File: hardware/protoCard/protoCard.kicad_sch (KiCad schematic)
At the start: 2 parts, among them J1 6502 Edge, J2 6502 Pinheader

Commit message: Protoboard v1.0
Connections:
- net NC36 is gone; now on net ~{RAM_CS}: J1.36 (Pin_36), J2.36 (Pin_36)
- net NC38 is gone; now on net A8: J1.38 (Pin_38), J2.38 (Pin_38)
- net NC40 is gone; now on net A10: J1.40 (Pin_40), J2.40 (Pin_40)
- net NC41 is gone; now on net A11: J1.41 (Pin_41), J2.41 (Pin_41)
- net ~{R0M_CS} is gone; now on net ~{NMI}: J1.19 (Pin_19), J2.19 (Pin_19)
- net A0: now also J1.6 (Pin_6), J2.6 (Pin_6); no longer J1.2 (Pin_2), J2.2 (Pin_2)
- net A1: now also J1.7 (Pin_7), J2.7 (Pin_7); no longer J1.3 (Pin_3), J2.3 (Pin_3)
- net A10: no longer J1.44 (Pin_44), J2.44 (Pin_44)
- net A11: no longer J1.45 (Pin_45), J2.45 (Pin_45)
- net A12: now also J1.42 (Pin_42), J2.42 (Pin_42); no longer J1.46 (Pin_46), J2.46 (Pin_46)
- net A13: now also J1.43 (Pin_43), J2.43 (Pin_43); no longer J1.47 (Pin_47), J2.47 (Pin_47)
- net A14: now also J1.44 (Pin_44), J2.44 (Pin_44); no longer J1.48 (Pin_48), J2.48 (Pin_48)
- net A15: now also J1.45 (Pin_45), J2.45 (Pin_45); no longer J1.49 (Pin_49), J2.49 (Pin_49)
- net A2: now also J1.8 (Pin_8), J2.8 (Pin_8); no longer J1.4 (Pin_4), J2.4 (Pin_4)
- net A3: now also J1.9 (Pin_9), J2.9 (Pin_9); no longer J1.5 (Pin_5), J2.5 (Pin_5)
- net A4: now also J1.10 (Pin_10), J2.10 (Pin_10); no longer J1.6 (Pin_6), J2.6 (Pin_6)
- net A5: now also J1.11 (Pin_11), J2.11 (Pin_11); no longer J1.7 (Pin_7), J2.7 (Pin_7)
- net A6: now also J1.12 (Pin_12), J2.12 (Pin_12); no longer J1.8 (Pin_8), J2.8 (Pin_8)
- net A7: now also J1.13 (Pin_13), J2.13 (Pin_13); no longer J1.9 (Pin_9), J2.9 (Pin_9)
- net A8: no longer J1.42 (Pin_42), J2.42 (Pin_42)
- net A9: now also J1.39 (Pin_39), J2.39 (Pin_39); no longer J1.43 (Pin_43), J2.43 (Pin_43)
- net D0: now also J1.5 (Pin_5), J2.5 (Pin_5); no longer J1.10 (Pin_10), J2.10 (Pin_10)
- net D1: now also J1.4 (Pin_4), J2.4 (Pin_4); no longer J1.11 (Pin_11), J2.11 (Pin_11)
- net D2: now also J1.3 (Pin_3), J2.3 (Pin_3); no longer J1.12 (Pin_12), J2.12 (Pin_12)
- net D3: now also J1.2 (Pin_2), J2.2 (Pin_2); no longer J1.13 (Pin_13), J2.13 (Pin_13)
- net D4: now also J1.49 (Pin_49), J2.49 (Pin_49); no longer J1.14 (Pin_14), J2.14 (Pin_14)
- net D5: now also J1.48 (Pin_48), J2.48 (Pin_48); no longer J1.15 (Pin_15), J2.15 (Pin_15)
- net D6: now also J1.47 (Pin_47), J2.47 (Pin_47); no longer J1.16 (Pin_16), J2.16 (Pin_16)
- net D7: now also J1.46 (Pin_46), J2.46 (Pin_46); no longer J1.17 (Pin_17), J2.17 (Pin_17)
- net GND: no longer J1.39 (Pin_39), J2.39 (Pin_39)
- net ~{IO_CS}: now also J1.20 (Pin_20), J2.20 (Pin_20); no longer J1.21 (Pin_21), J2.21 (Pin_21)
- net ~{NMI}: no longer J1.20 (Pin_20), J2.20 (Pin_20)
- net ~{RAM_CS}: no longer J1.33 (Pin_33), J2.33 (Pin_33)
- net ~{RD}: now also J1.16 (Pin_16), J2.16 (Pin_16); no longer J1.34 (Pin_34), J2.34 (Pin_34)
- new net NC14: J1.14 (Pin_14), J2.14 (Pin_14)
- new net NC15: J1.15 (Pin_15), J2.15 (Pin_15)
- new net NC33: J1.33 (Pin_33), J2.33 (Pin_33)
- new net NC34: J1.34 (Pin_34), J2.34 (Pin_34)
- new net ~{IO_08}: J1.21 (Pin_21), J2.21 (Pin_21)
- new net ~{ROM_CS}: J1.17 (Pin_17), J2.17 (Pin_17)
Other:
- company: (none) -> MDS
- title: (none) -> Protoboard Card

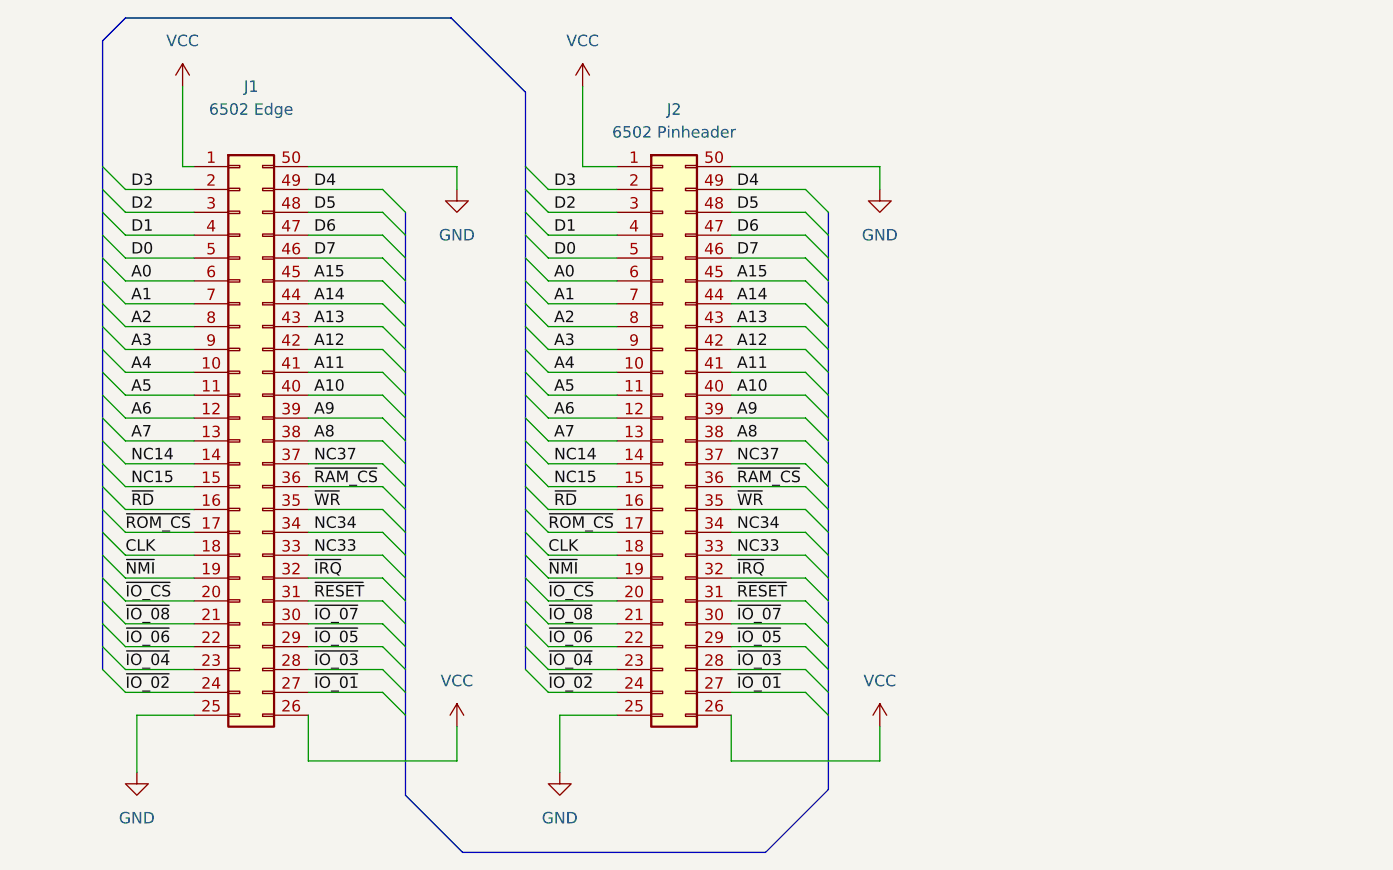
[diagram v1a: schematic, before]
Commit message: fixed pinout + power led
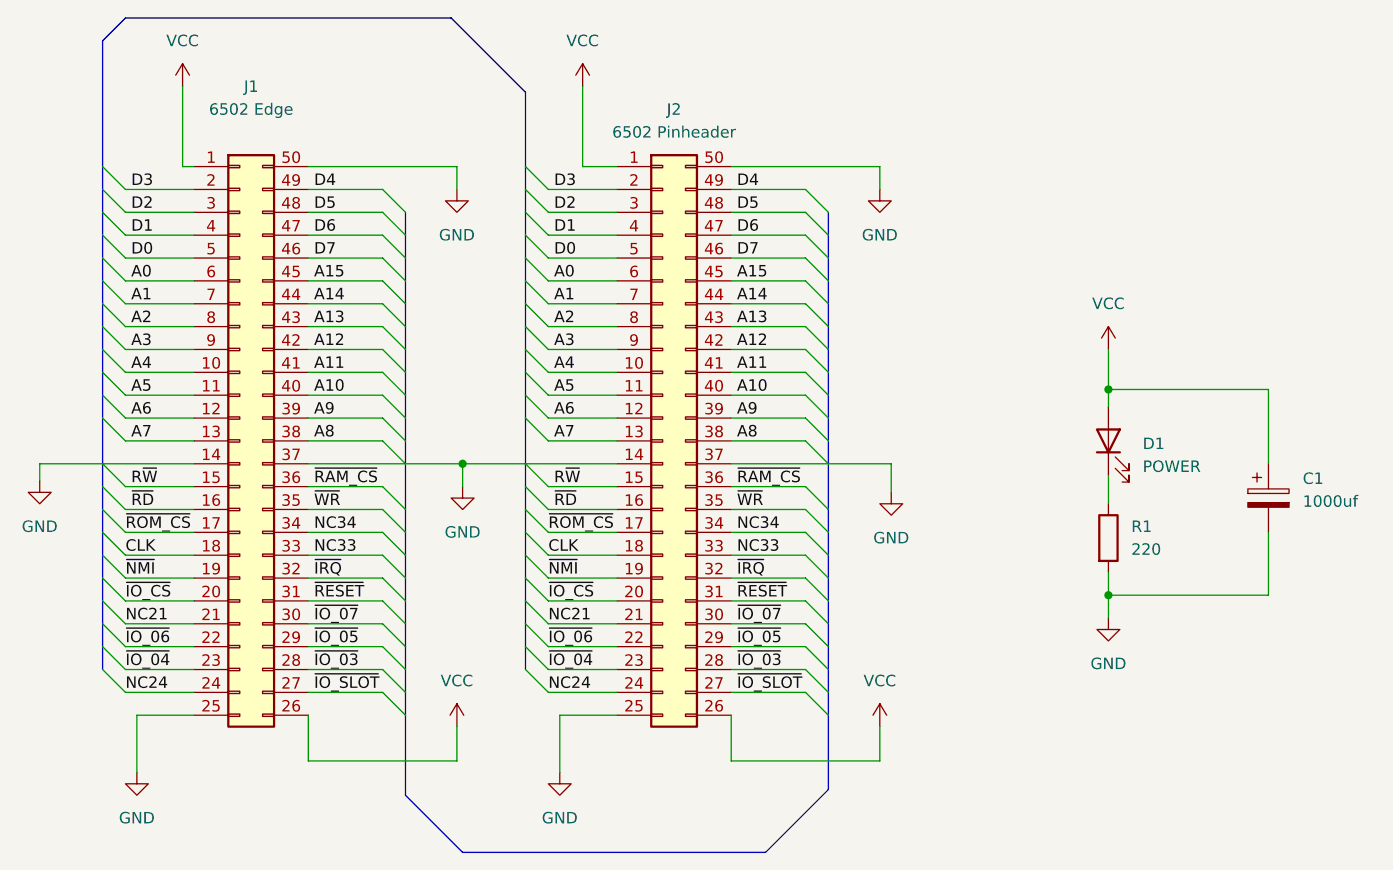
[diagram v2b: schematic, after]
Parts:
- added C1: 1000uf, Capacitor_THT:CP_Radial_D5.0mm_P2.50mm, symbol Device:C_Polarized
- added D1: POWER, LED_THT:LED_D3.0mm, symbol Device:LED
- added R1: 220, Resistor_THT:R_Axial_DIN0207_L6.3mm_D2.5mm_P10.16mm_Horizontal, symbol Device:R
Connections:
- net NC14 is gone; now on net GND: J1.14 (Pin_14), J2.14 (Pin_14)
- net NC37 is gone; now on net GND: J1.37 (Pin_37), J2.37 (Pin_37)
- net GND: now also C1.2, R1.2
- net VCC: now also C1.1, D1.2 (A)
- net NC15 renamed R~{W}
- net ~{IO_01} renamed ~{IO_SLOT}
- net ~{IO_02} renamed NC24
- net ~{IO_08} renamed NC21
- new net: D1.1 (K), R1.1
